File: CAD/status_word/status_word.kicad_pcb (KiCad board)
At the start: 2 copper layers, 70 x 39 mm, 46 parts, among them J1 Conn_01x26_Pin, U1 74HC161, U2 74HC109, U3 74HC157, U4 74HC157, U5 74HC245, U6 74HC02

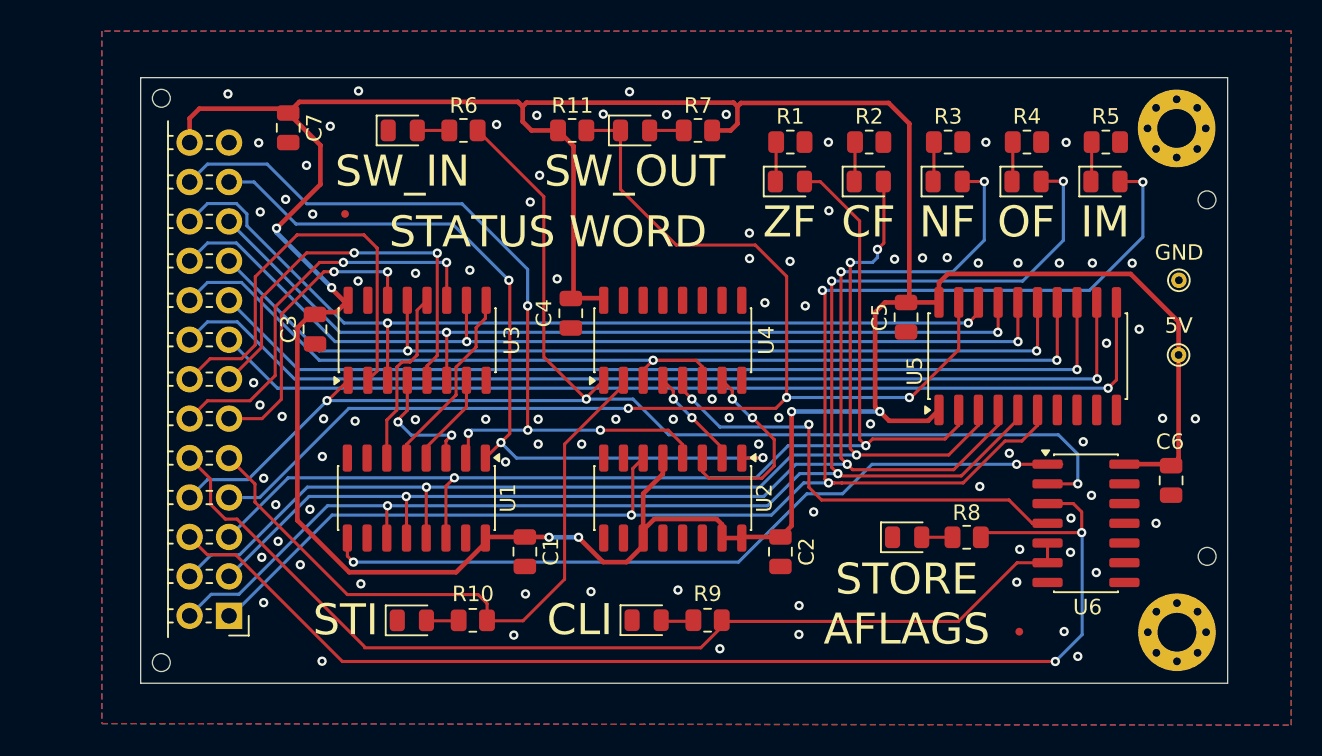
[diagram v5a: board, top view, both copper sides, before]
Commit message: change buffer footprint in SW
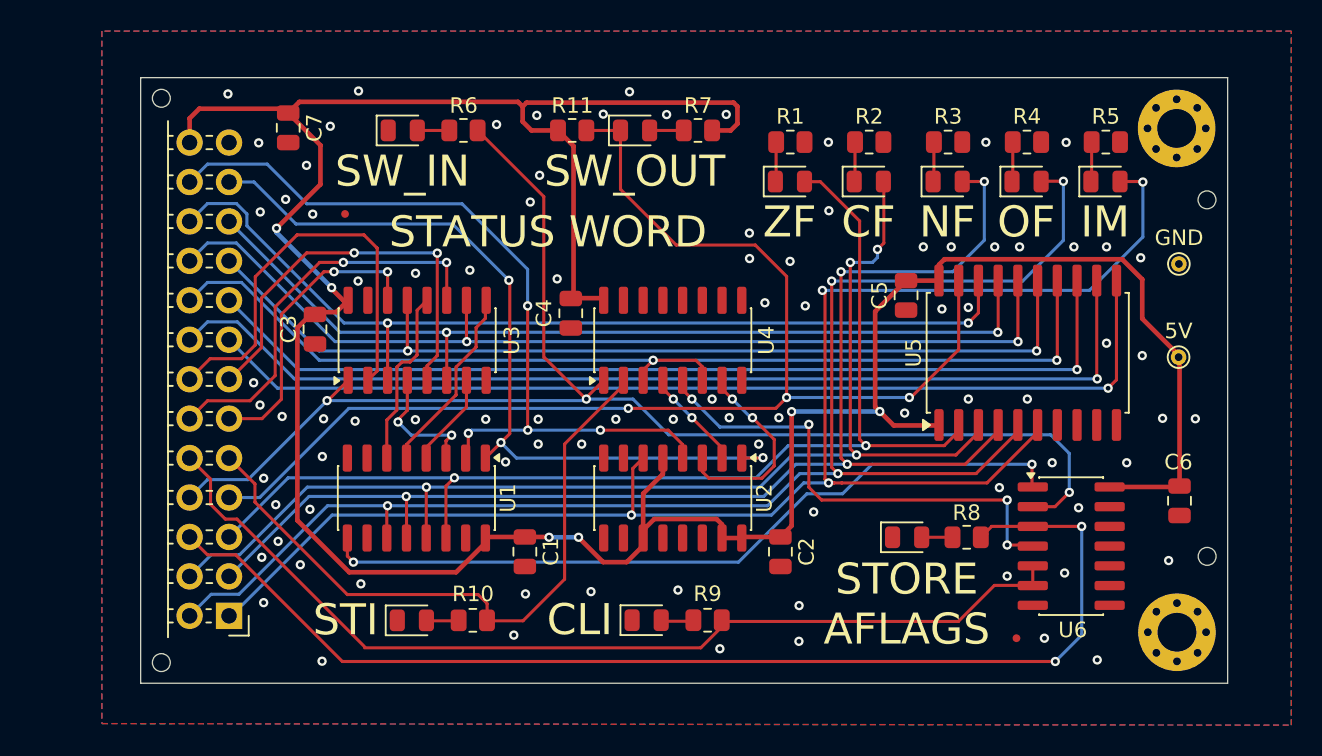
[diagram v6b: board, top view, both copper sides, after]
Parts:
- U5: footprint Package_SO:SO-20_5.3x12.6mm_P1.27mm -> Package_SO:SOIC-20W_7.5x12.8mm_P1.27mm
- moved U6 1.75 mm to (113.9, 69.2)
- moved C6 1.42 mm to (120.9, 66.2)
- moved C5 1.41 mm to (103.3, 53.0)
- moved TP2 1.05 mm to (120.9, 51.0)
- moved FID2 0.46 mm to (110.4, 75.1)
- moved U5 0.22 mm to (111.1, 56.7)
- moved TP1 0.14 mm to (120.8, 57.0)
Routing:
- net +5V: track 213.6 -> 194.1 mm
- net aflags_in: track 78.1 -> 75.5 mm
- net /dbus0: track 58.9 -> 60.9 mm
- net Net-(U4-I0b): track 29.6 -> 31.2 mm, vias 2 -> 4
- net /sw.nf: track 85.4 -> 83.9 mm
- net ~{sw_out}: track 80.8 -> 82.2 mm
- net /dbus7: track 63.7 -> 65.1 mm
- net /dbus6: track 65.4 -> 66.8 mm
- net /dbus5: track 60.8 -> 62.2 mm
- net /dbus3: track 60.8 -> 62.2 mm
- net /dbus2: track 61.7 -> 63.1 mm
- net /dbus1: track 57.5 -> 58.9 mm
- net /dbus4: track 67.3 -> 68.7 mm
- net /sw.cf: track 78.0 -> 76.9 mm
- net cli: track 64.3 -> 63.2 mm
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
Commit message: CLK test point, CC-BY-NC-SA
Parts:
- added Ref**: Val**, 8-bit_computer:by-nc-sa.eu, B.Cu at (76.7, 73.2)
- added TP3: TestPoint, TestPoint:TestPoint_THTPad_D1.0mm_Drill0.5mm, F.Cu at (76.7, 46.4)
- added TP4: TestPoint, TestPoint:TestPoint_THTPad_D1.0mm_Drill0.5mm, F.Cu at (80.5, 51.0)
- moved G*** 1.87 mm to (88.3, 48.6)
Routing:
- net clk: track 52.0 -> 54.3 mm
- net /sw.vf: track 94.9 -> 94.1 mm
- net Net-(U2A-~{K}): track 13.0 -> 12.4 mm
- net Net-(U2A-J): track 5.93 -> 5.39 mm
- net GND: vias 89 -> 87
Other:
- board text added: "CLK"

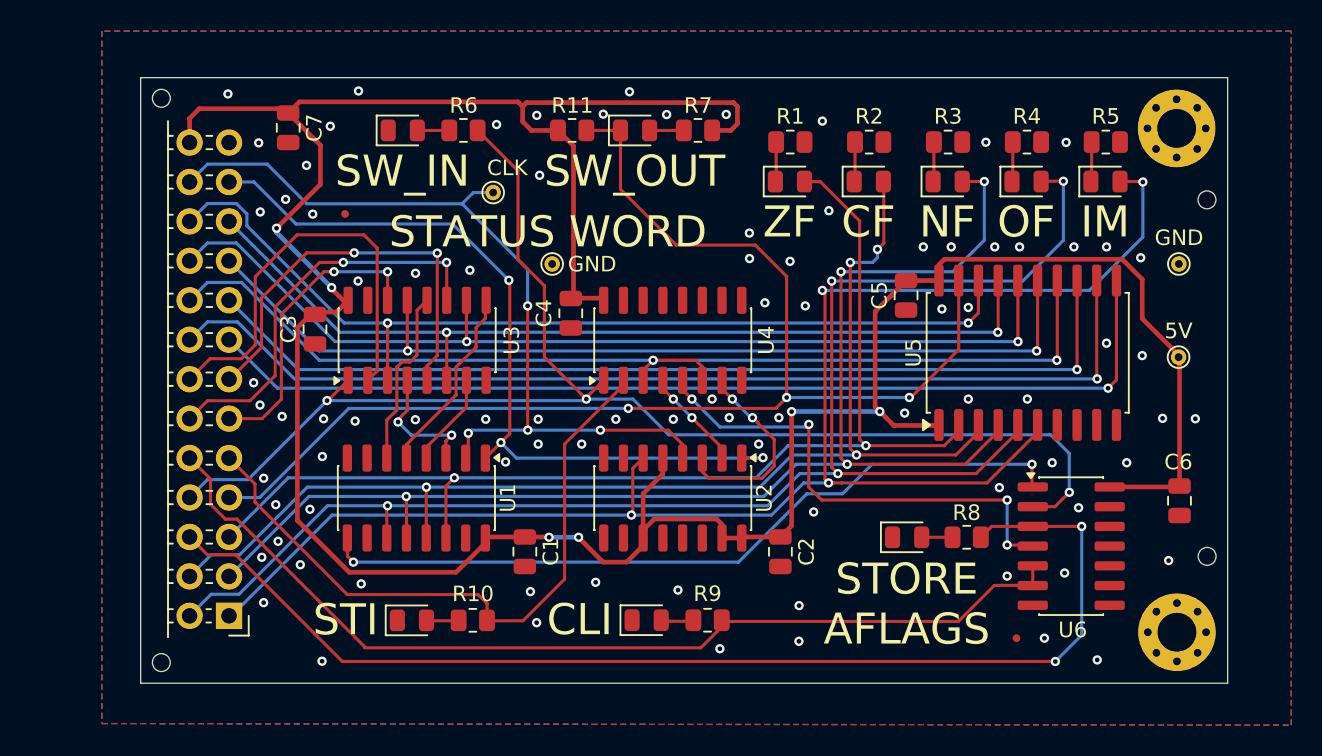
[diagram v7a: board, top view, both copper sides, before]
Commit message: update SW, add footprints and 3D models to library
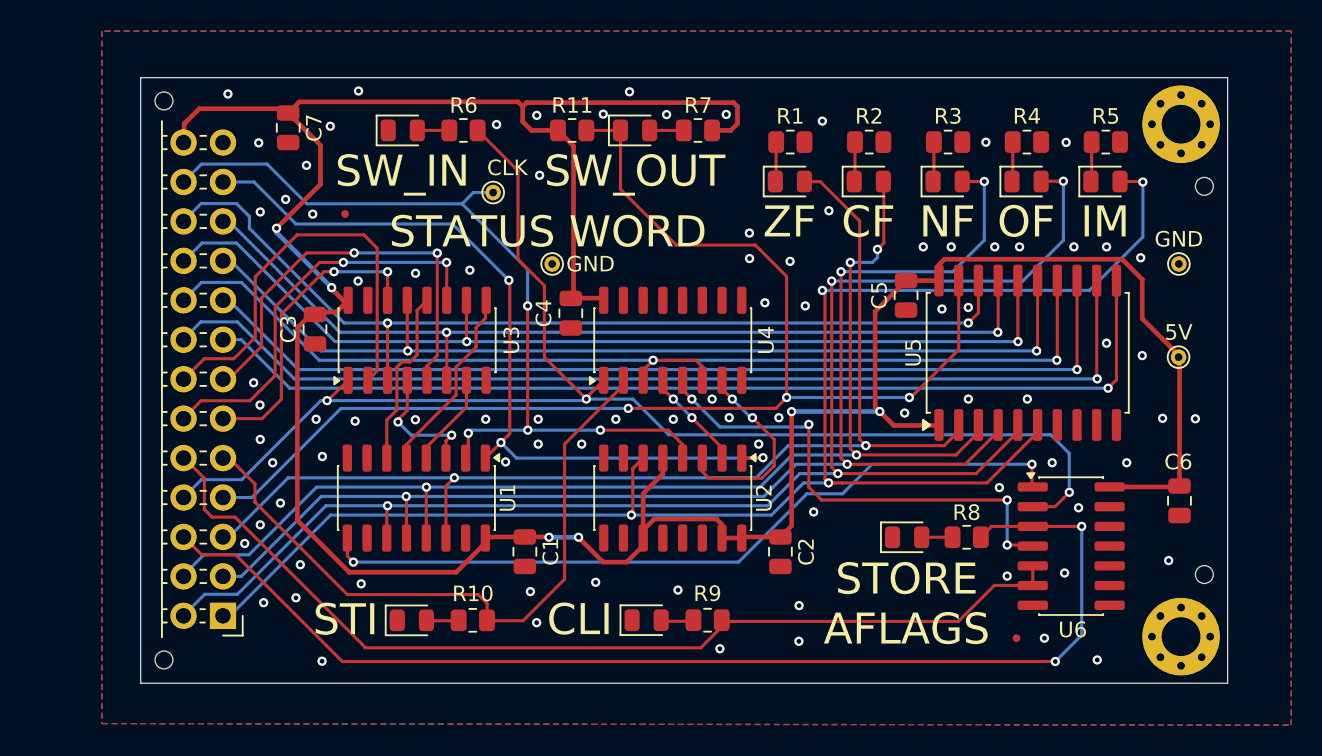
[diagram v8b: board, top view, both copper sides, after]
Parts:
- removed the G*** at (88.3, 48.6)
- added G***: LOGO, 8-bit_computer:qr-code-github, B.Cu at (88.3, 48.7)
- moved H6 1.18 mm to (122.5, 71.0)
- moved H5 0.89 mm to (122.5, 46.0)
- moved H1 0.39 mm to (121.0, 42.0)
- moved J1 0.39 mm to (59.3, 73.7)
- moved H2 0.39 mm to (121.0, 75.0)
- moved H3 0.24 mm to (55.5, 40.5)
- moved H4 0.24 mm to (55.5, 76.5)
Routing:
- net cli: track 63.2 -> 63.8 mm
- net /aflags.cf: track 27.1 -> 27.6 mm
- net /sw.im: track 100.5 -> 101.0 mm
